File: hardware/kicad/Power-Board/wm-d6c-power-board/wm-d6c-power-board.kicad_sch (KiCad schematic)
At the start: 30 parts, among them J3 USB_C_Receptacle, J4 Barrel_Jack, U6 AP63203WU-7, U7 IP2721, U8 MT3608, U9 MCP1700x-330xxTT

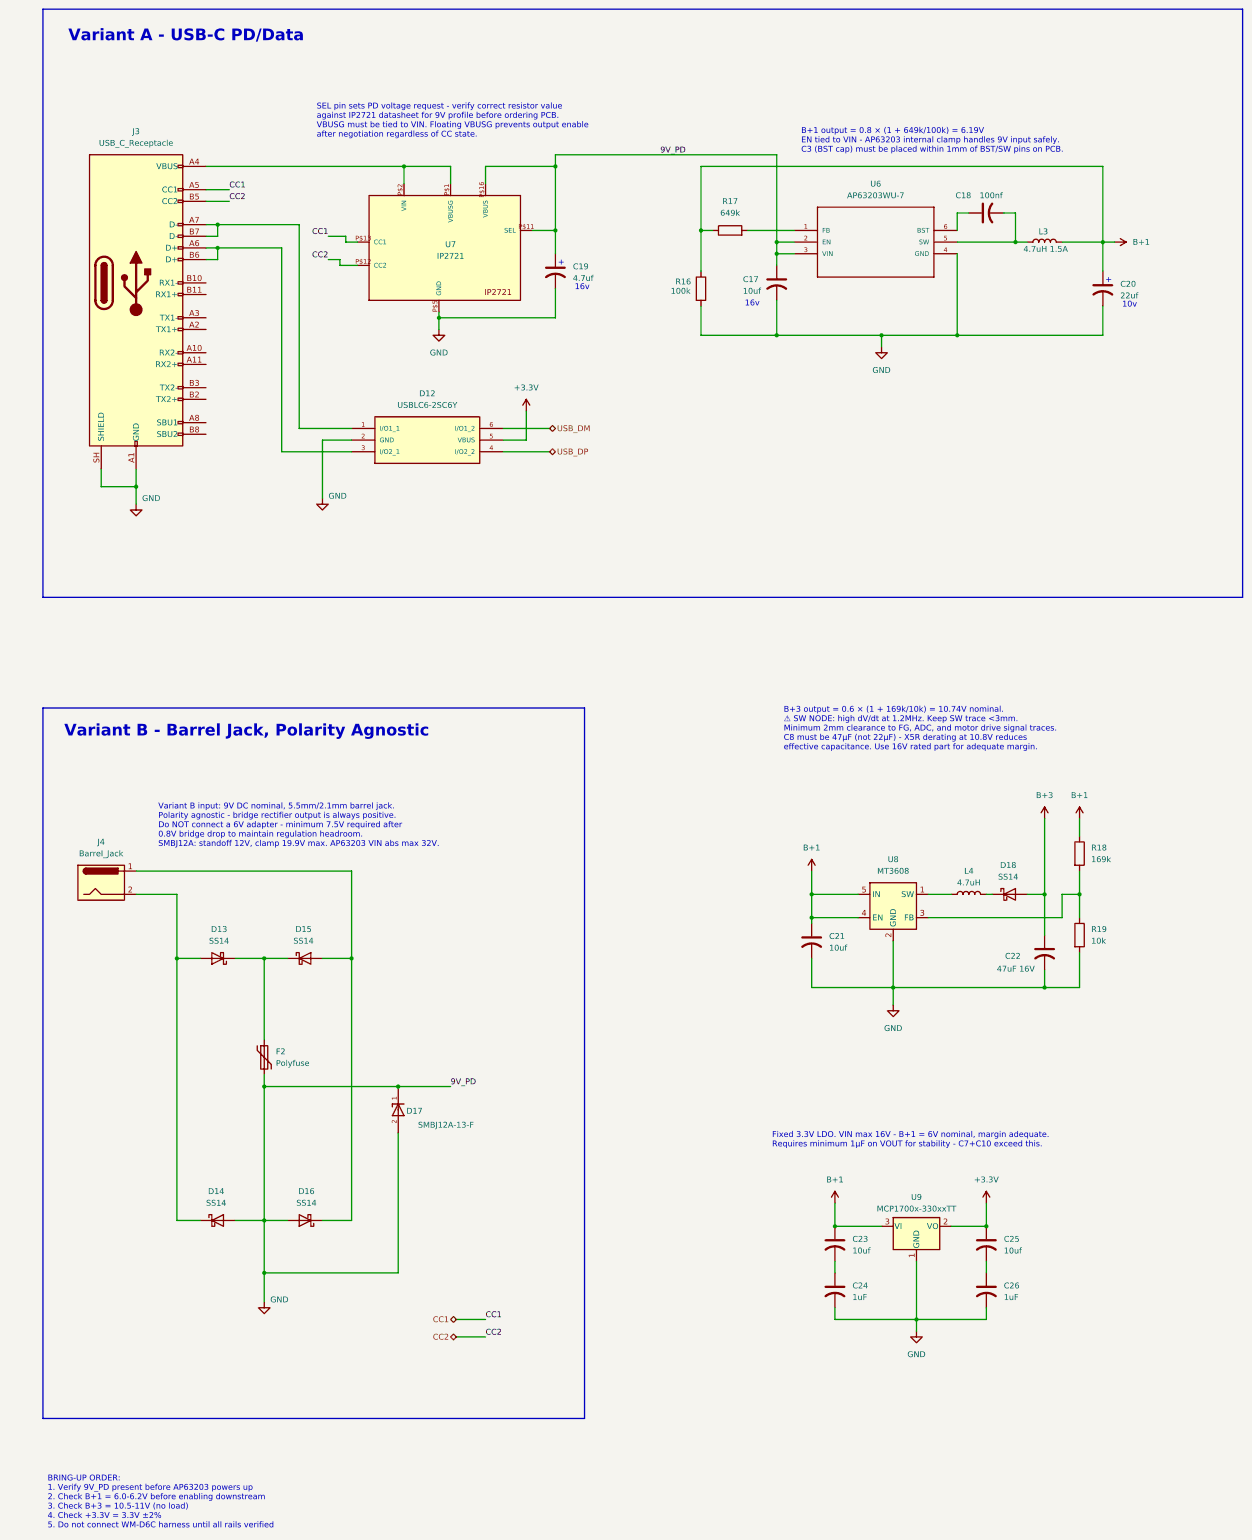
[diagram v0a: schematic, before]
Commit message: updated schematics
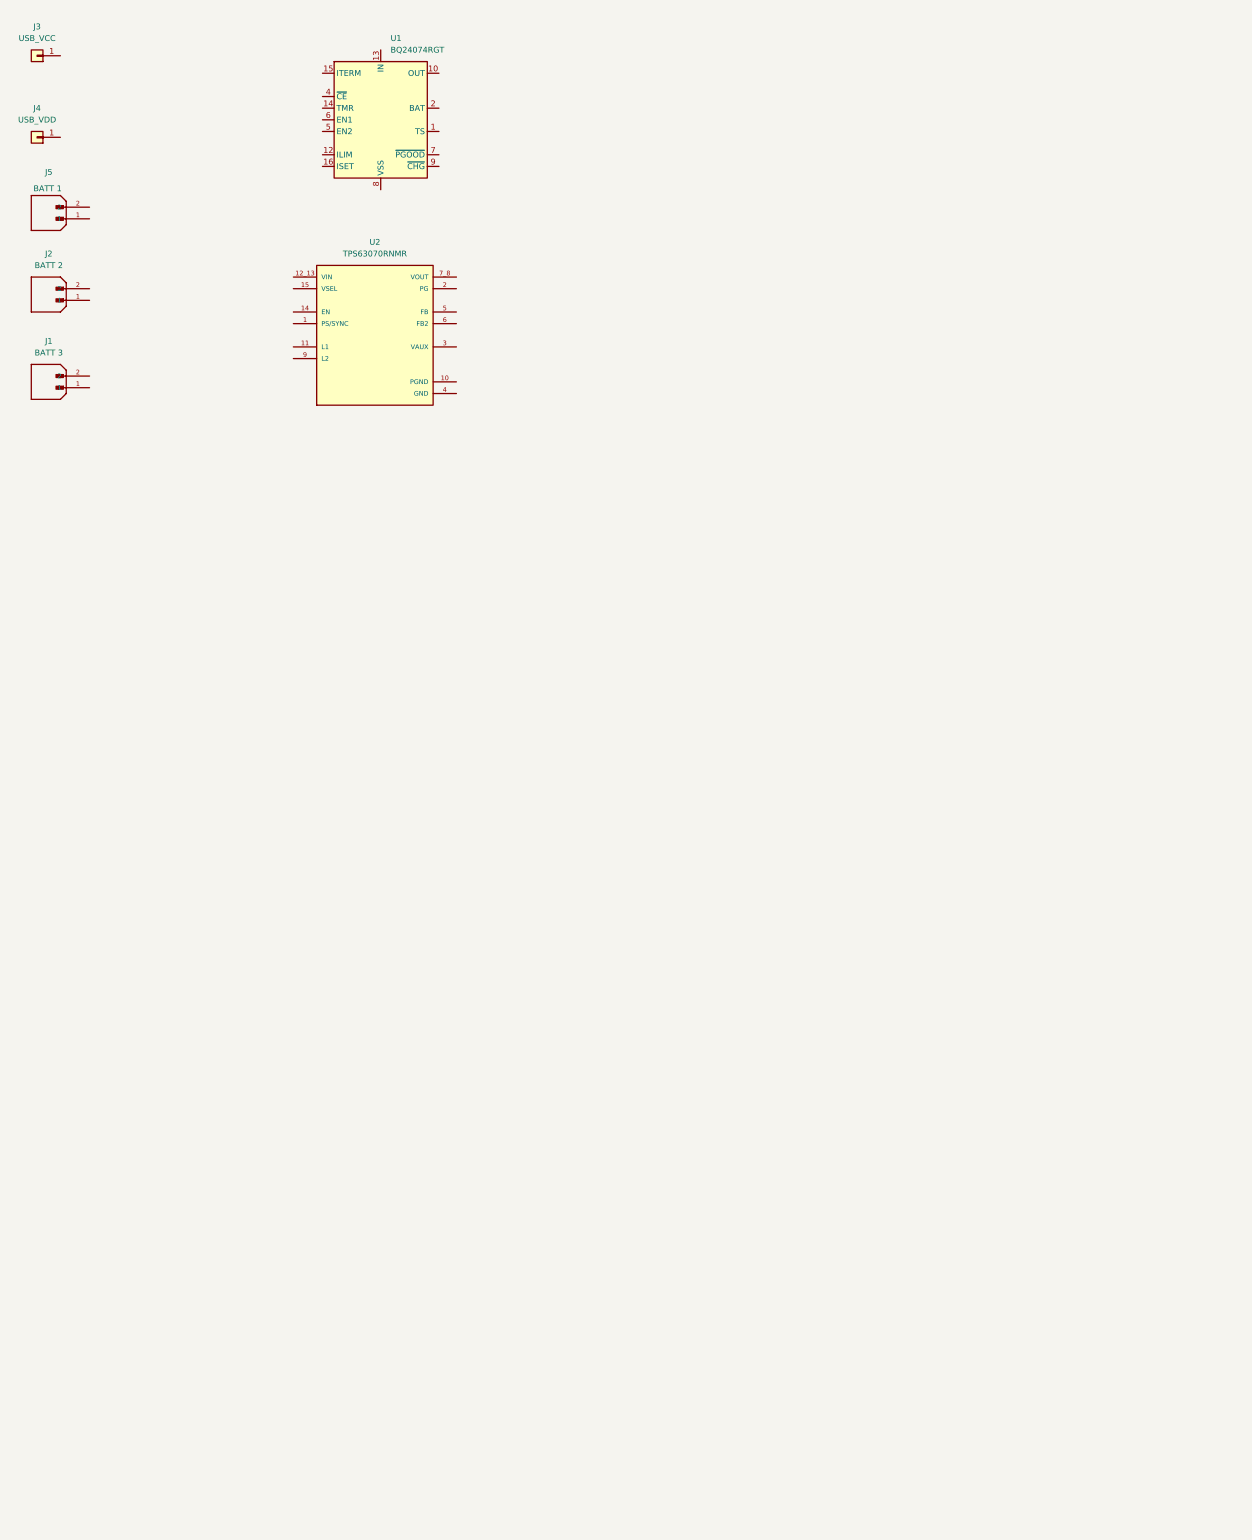
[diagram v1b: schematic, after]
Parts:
- removed C17, C21, C23, C25: 10uf, symbol Device:C_US
- removed C18: 100nf, symbol Device:C_US
- removed C19: 4.7uf, symbol Device:C_US
- removed C20: 22uf, symbol Device:C_US
- removed C22: 47uF 16V, symbol Device:C_US
- removed C24, C26: 1uF, symbol Device:C_US
- removed D12: USBLC6-2SC6Y, USBLC6-2SC6Y:SOT95P280X145-6N, symbol DSR-1:USBLC6-2SC6Y
- removed D13, D14, D15, D16, D18: SS14, Diode_SMD:D_SMA, symbol Diode:SS14
- removed D17: SMBJ12A-13-F, SMBJ12A-13-F:DIOM5336X250N, symbol SMBJ12A-13-F:SMBJ12A-13-F
- removed F2: Polyfuse, symbol Device:Polyfuse
- removed J3: USB_C_Receptacle, symbol DSR-1:USB_C_Receptacle
- removed J4: Barrel_Jack, symbol Connector:Barrel_Jack
- removed L3: 4.7uH 1.5A, symbol Device:L
- removed L4: 4.7uH, symbol Device:L
- removed R16: 100k, symbol Device:R
- removed R17: 649k, symbol Device:R
- removed R18: 169k, symbol Device:R
- removed R19: 10k, symbol Device:R
- removed U6: AP63203WU-7, AP63203WU-7:SOIC_05WU-7_DIO-M, symbol AP63203WU-7:AP63203WU-7
- removed U7: IP2721, IP2721:TSSOP16, symbol DSR-1:IP2721
- removed U8: MT3608, Package_TO_SOT_SMD:SOT-23-6, symbol DSR-1:MT3608
- removed U9: MCP1700x-330xxTT, Package_TO_SOT_SMD:SOT-23, symbol DSR-1:MCP1700x-330xxTT
- added J1: BATT 3, B2B-PH-SM4-TB:JST_B2B-PH-SM4-TB, symbol B2B-PH-SM4-TB:B2B-PH-SM4-TB
- added J2: BATT 2, B2B-PH-SM4-TB:JST_B2B-PH-SM4-TB, symbol B2B-PH-SM4-TB:B2B-PH-SM4-TB
- added J3: USB_VCC, symbol Connector_Generic:Conn_01x01
- added J4: USB_VDD, symbol Connector_Generic:Conn_01x01
- added J5: BATT 1, B2B-PH-SM4-TB:JST_B2B-PH-SM4-TB, symbol B2B-PH-SM4-TB:B2B-PH-SM4-TB
- added U1: BQ24074RGT, Package_DFN_QFN:VQFN-16-1EP_3x3mm_P0.5mm_EP1.6x1.6mm, symbol Battery_Management:BQ24074RGT
- added U2: TPS63070RNMR, TPS63070RNMR:VREG_TPS63070RNMR, symbol TPS63070RNMR:TPS63070RNMR
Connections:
- new net: U1.10 (OUT), U1.11 (OUT)
- new net: U1.17 (VSS), U1.8 (VSS)
- new net: U1.2 (BAT), U1.3 (BAT)
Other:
- note removed: "+"
- note removed: "10v"
- note removed: "16v"
- note removed: "B+1 output = 0.8 × (1 + 649k/100k) = 6.19V EN tied to VIN - AP63203 internal clamp handles 9V input safely. C3 (BST cap) must be placed within 1mm of BST/SW pins on PCB."
- note removed: "B+3 output = 0.6 × (1 + 169k/10k) = 10.74V nominal. ⚠ SW NODE: high dV/dt at 1.2MHz. Keep SW trace <3mm. Minimum 2mm clearance to FG, ADC, and motor drive signal traces. C8 must be 47µF (not 22µF) - X5R derating at 10.8V reduces effective capacitance. Use 16V rated part for adequate margin."
- note removed: "BRING-UP ORDER: 1. Verify 9V_PD present before AP63203 powers up 2. Check B+1 = 6.0-6.2V before enabling downstream 3. Check B+3 = 10.5-11V (no load) 4. Check +3.3V = 3.3V ±2% 5. Do not connect WM-D6C harness until all rails verified"
- note removed: "Fixed 3.3V LDO. VIN max 16V - B+1 = 6V nominal, margin adequate. Requires minimum 1µF on VOUT for stability - C7+C10 exceed this."
- note removed: "SEL pin sets PD voltage request - verify correct resistor value against IP2721 datasheet for 9V profile before ordering PCB. VBUSG must be tied to VIN. Floating VBUSG prevents output enable after negotiation regardless of CC state."
- note removed: "Variant A - USB-C PD/Data"
- note removed: "Variant B - Barrel Jack, Polarity Agnostic"
- note removed: "Variant B input: 9V DC nominal, 5.5mm/2.1mm barrel jack. Polarity agnostic - bridge rectifier output is always positive. Do NOT connect a 6V adapter - minimum 7.5V required after 0.8V bridge drop to maintain regulation headroom. SMBJ12A: standoff 12V, clamp 19.9V max. AP63203 VIN abs max 32V."
